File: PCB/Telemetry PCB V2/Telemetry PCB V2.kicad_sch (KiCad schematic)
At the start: 51 parts, among them IC1 E22-900M33S, J1 USB_C_Receptacle_USB2.0_16P, J2 DBG/PGRM Hdr., J3 DATA IN, J4 GPS, J5 Battery, SW1 BOOT, SW2 RESET, U1 STM32F411CEUx, U2 MCP1700x-250xxTT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

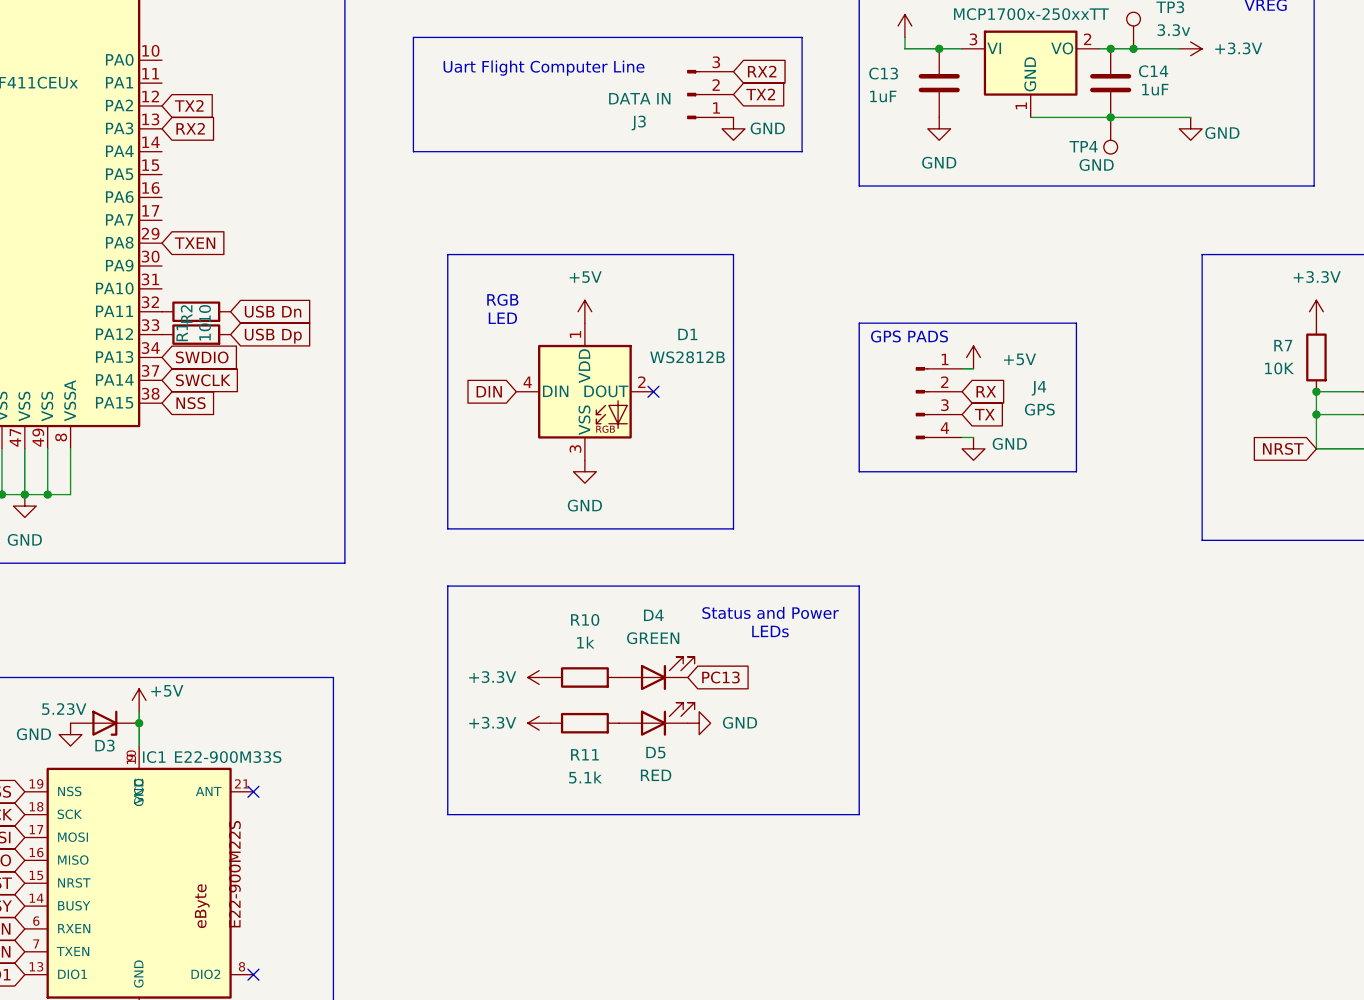
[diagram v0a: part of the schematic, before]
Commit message: Added buzzer header
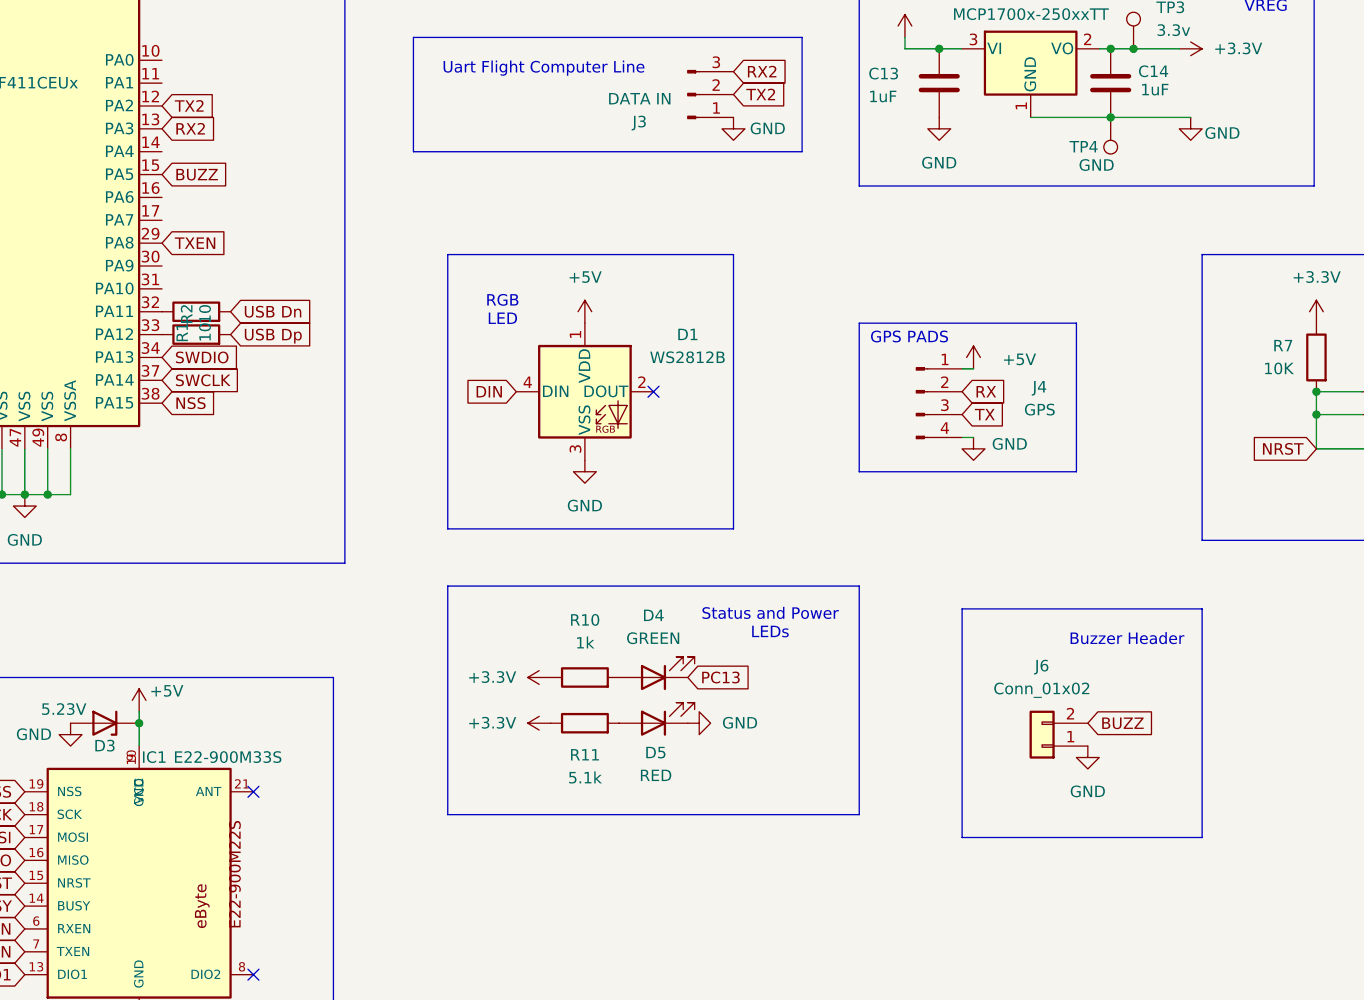
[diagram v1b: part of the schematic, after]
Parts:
- added J6: Conn_01x02, Connector_JST:JST_XH_B2B-XH-A_1x02_P2.50mm_Vertical, symbol Connector_Generic:Conn_01x02
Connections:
- net GND: now also J6.1 (Pin_1)
- net BUZZ: now reaches U1.15 (PA5)
- net BUZZ: now also J6.2 (Pin_2)
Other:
- note added: "Buzzer Header"
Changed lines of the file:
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@@
 	)
 	(rectangle
+		(start 205.74 132.08)
+		(end 232.41 157.48)
+		(stroke
+			(width 0)
+			(type default)
+		)
+		(fill
+			(type none)
+		)
+	)
+	(rectangle
 		(start 30.48 14.605)
 		(end 137.16 127)
@@
 		)
 	)
+	(text "Buzzer Header"
+		(exclude_from_sim no)
+		(at 224.028 135.636 0)
+		(effects
+			(font
+				(size 1.27 1.27)
+			)
+		)
+	)
 	(text "Status and Power\nLEDs\n"
 		(exclude_from_sim no)
@@
 		)
 	)
+	(global_label "BUZZ"
+		(shape input)
+		(at 219.71 144.78 0)
+		(fields_autoplaced yes)
+		(effects
+			(font
+				(size 1.27 1.27)
+			)
+			(justify left)
+		)
+		(property "Intersheetrefs" "${INTERSHEET_REFS}"
+			(at 227.7147 144.78 0)
+			(effects
+				(font
+					(size 1.27 1.27)
+				)
+				(justify left)
+				(hide yes)
+			)
+		)
+	)
 	(global_label "NSS"
 		(shape input)
@@
 		)
 	)
+	(global_label "BUZZ"
+		(shape input)
+		(at 116.84 83.82 0)
+		(fields_autoplaced yes)
+		(effects
+			(font
+				(size 1.27 1.27)
+			)
+			(justify left)
+		)
+		(property "Intersheetrefs" "${INTERSHEET_REFS}"
+			(at 124.8447 83.82 0)
+			(effects
+				(font
+					(size 1.27 1.27)
+				)
+				(justify left)
+				(hide yes)
+			)
+		)
+	)
 	(global_label "RXEN"
 		(shape input)
@@
 	)
 	(symbol
+		(lib_name "GND_20")
+		(lib_id "power:GND")
+		(at 219.71 147.32 0)
+		(unit 1)
+		(exclude_from_sim no)
+		(in_bom yes)
+		(on_board yes)
+		(dnp no)
+		(fields_autoplaced yes)
+		(property "Reference" "#PWR034"
+			(at 219.71 153.67 0)
+			(effects
+				(font
+					(size 1.27 1.27)
+				)
+				(hide yes)
+			)
+		)
+		(property "Value" "GND"
+			(at 219.71 152.4 0)
+			(effects
+				(font
+					(size 1.27 1.27)
+				)
+			)
+		)
+		(property "Footprint" ""
+			(at 219.71 147.32 0)
+			(effects
+				(font
+					(size 1.27 1.27)
+				)
+				(hide yes)
+			)
+		)
+		(property "Datasheet" ""
+			(at 219.71 147.32 0)
+			(effects
+				(font
+					(size 1.27 1.27)
+				)
+				(hide yes)
+			)
+		)
+		(property "Description" "Power symbol creates a global label with name \"GND\" , ground"
+			(at 219.71 147.32 0)
+			(effects
+				(font
+					(size 1.27 1.27)
+				)
+				(hide yes)
+			)
+		)
+		(pin "1"
+		)
+		(instances
+			(project ""
+				(path "/d3e58202-7594-4bd8-a3d4-cb0300333d9c"
+					(reference "#PWR034")
+					(unit 1)
+				)
+			)
+		)
+	)
+	(symbol
 		(lib_id "power:+5V")
 		(at 264.16 43.18 270)
@@
 					(unit 1)
 				)
+			)
+		)
+	)
+	(symbol
+		(lib_id "Connector_Generic:Conn_01x02")
+		(at 214.63 147.32 180)
+		(unit 1)
+		(exclude_from_sim no)
+		(in_bom yes)
+		(on_board yes)
+		(dnp no)
+		(fields_autoplaced yes)
+		(property "Reference" "J6"
+			(at 214.63 138.43 0)
+			(effects
+				(font
+					(size 1.27 1.27)
+				)
+			)
+		)
+		(property "Value" "Conn_01x02"
+			(at 214.63 140.97 0)
+			(effects
+				(font
+					(size 1.27 1.27)
+				)
+			)
+		)
+		(property "Footprint" "Connector_JST:JST_XH_B2B-XH-A_1x02_P2.50mm_Vertical"
+			(at 214.63 147.32 0)
+			(effects
+				(font
+					(size 1.27 1.27)
+				)
+				(hide yes)
+			)
+		)
+		(property "Datasheet" "~"
+			(at 214.63 147.32 0)
+			(effects
+				(font
+					(size 1.27 1.27)
+				)
+				(hide yes)
+			)
+		)
+		(property "Description" "Generic connector, single row, 01x02, script generated (kicad-library-utils/schlib/autogen/connector/)"
+			(at 214.63 147.32 0)
+			(effects
+				(font
+					(size 1.27 1.27)
+				)
+				(hide yes)
+			)
+		)
+		(pin "2"
+		)
+		(pin "1"
+		)
+		(instances
+			(project ""
+				(path "/d3e58202-7594-4bd8-a3d4-cb0300333d9c"
+					(reference "J6")
+					(unit 1)
+				)

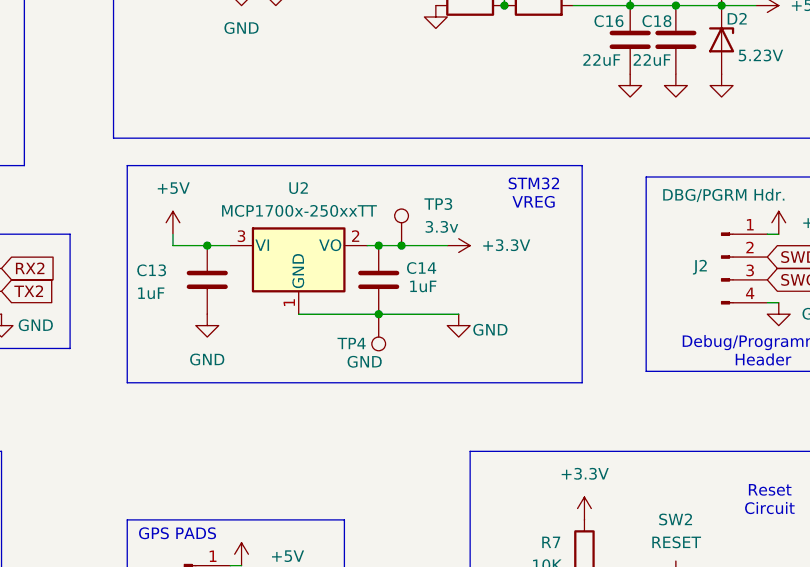
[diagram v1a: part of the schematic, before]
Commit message: Added Graphics
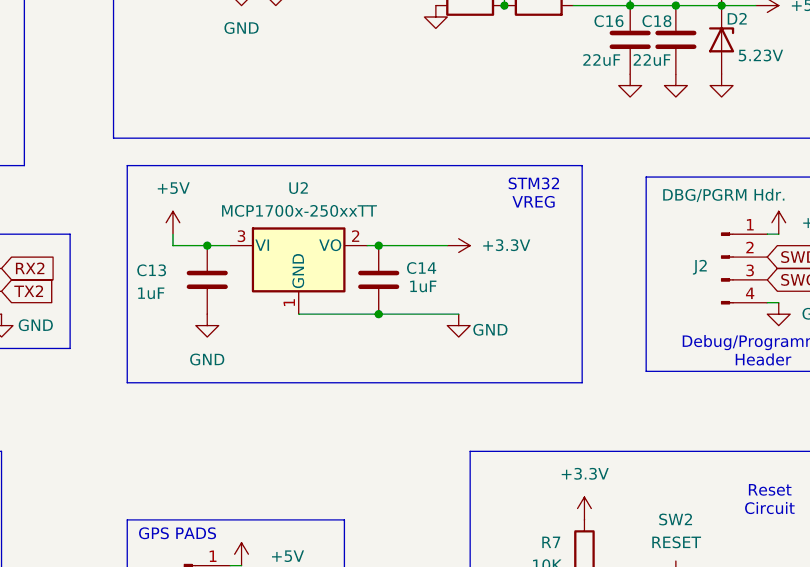
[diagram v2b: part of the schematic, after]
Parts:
- removed TP3: 3.3v, TestPoint:TestPoint_Loop_D1.80mm_Drill1.0mm_Beaded, symbol Connector:TestPoint
- removed TP4: GND, TestPoint:TestPoint_Loop_D1.80mm_Drill1.0mm_Beaded, symbol Connector:TestPoint
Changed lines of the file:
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@@
 	)
 	(junction
-		(at 224.79 69.85)
-		(diameter 0)
-		(color 0 0 0 0)
-	)
-	(junction
 		(at 102.87 33.02)
 		(diameter 0)
@@
 	(wire
 		(pts
-			(xy 222.25 69.85) (xy 224.79 69.85)
+			(xy 222.25 69.85) (xy 229.87 69.85)
 		)
 		(stroke
@@
 	(wire
 		(pts
-			(xy 224.79 69.85) (xy 229.87 69.85)
-		)
-		(stroke
-			(width 0)
-			(type default)
-		)
-	)
-	(wire
-		(pts
 			(xy 106.68 35.56) (xy 106.68 33.02)
 		)
@@
 	)
 	(symbol
-		(lib_id "Connector:TestPoint")
-		(at 222.25 77.47 180)
-		(unit 1)
-		(exclude_from_sim no)
-		(in_bom yes)
-		(on_board yes)
-		(dnp no)
-		(property "Reference" "TP4"
-			(at 217.678 80.772 0)
-			(effects
-				(font
-					(size 1.27 1.27)
-				)
-				(justify right)
-			)
-		)
-		(property "Value" "GND"
-			(at 218.694 82.804 0)
-			(effects
-				(font
-					(size 1.27 1.27)
-				)
-				(justify right)
-			)
-		)
-		(property "Footprint" "TestPoint:TestPoint_Loop_D1.80mm_Drill1.0mm_Beaded"
-			(at 217.17 77.47 0)
-			(effects
-				(font
-					(size 1.27 1.27)
-				)
-				(hide yes)
-			)
-		)
-		(property "Datasheet" "~"
-			(at 217.17 77.47 0)
-			(effects
-				(font
-					(size 1.27 1.27)
-				)
-				(hide yes)
-			)
-		)
-		(property "Description" "test point"
-			(at 222.25 77.47 0)
-			(effects
-				(font
-					(size 1.27 1.27)
-				)
-				(hide yes)
-			)
-		)
-		(pin "1"
-		)
-		(instances
-			(project "Telemetry PCB V2"
-				(path "/d3e58202-7594-4bd8-a3d4-cb0300333d9c"
-					(reference "TP4")
-					(unit 1)
-				)
-			)
-		)
-	)
-	(symbol
 		(lib_id "Device:D_Zener")
 		(at 110.49 144.78 180)
@@
 					(unit 1)
 				)
-			)
-		)
-	)
-	(symbol
-		(lib_id "Connector:TestPoint")
-		(at 224.79 69.85 0)
-		(unit 1)
-		(exclude_from_sim no)
-		(in_bom yes)
-		(on_board yes)
-		(dnp no)
-		(fields_autoplaced yes)
-		(property "Reference" "TP3"
-			(at 227.33 65.2779 0)
-			(effects
-				(font
-					(size 1.27 1.27)
-				)
-				(justify left)
-			)
-		)
-		(property "Value" "3.3v"
-			(at 227.33 67.8179 0)
-			(effects
-				(font
-					(size 1.27 1.27)
-				)
-				(justify left)
-			)
-		)
-		(property "Footprint" "TestPoint:TestPoint_Loop_D1.80mm_Drill1.0mm_Beaded"
-			(at 229.87 69.85 0)
-			(effects
-				(font
-					(size 1.27 1.27)
-				)
-				(hide yes)
-			)
-		)
-		(property "Datasheet" "~"
-			(at 229.87 69.85 0)
-			(effects
-				(font
-					(size 1.27 1.27)
-				)
-				(hide yes)
-			)
-		)
-		(property "Description" "test point"
-			(at 224.79 69.85 0)
-			(effects
-				(font
-					(size 1.27 1.27)
-				)
-				(hide yes)
-			)
-		)
-		(pin "1"
-		)
-		(instances
-			(project ""
-				(path "/d3e58202-7594-4bd8-a3d4-cb0300333d9c"
-					(reference "TP3")
-					(unit 1)
-				)
